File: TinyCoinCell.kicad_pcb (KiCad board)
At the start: 4 copper layers, 23.8 x 24 mm, 51 parts, among them SW1 SW_Push, U1 nRF54L15-QFAA, U2 ADXL367, U8 nPM2100-QEXX, X1 32MHz, X2 32.768kHz

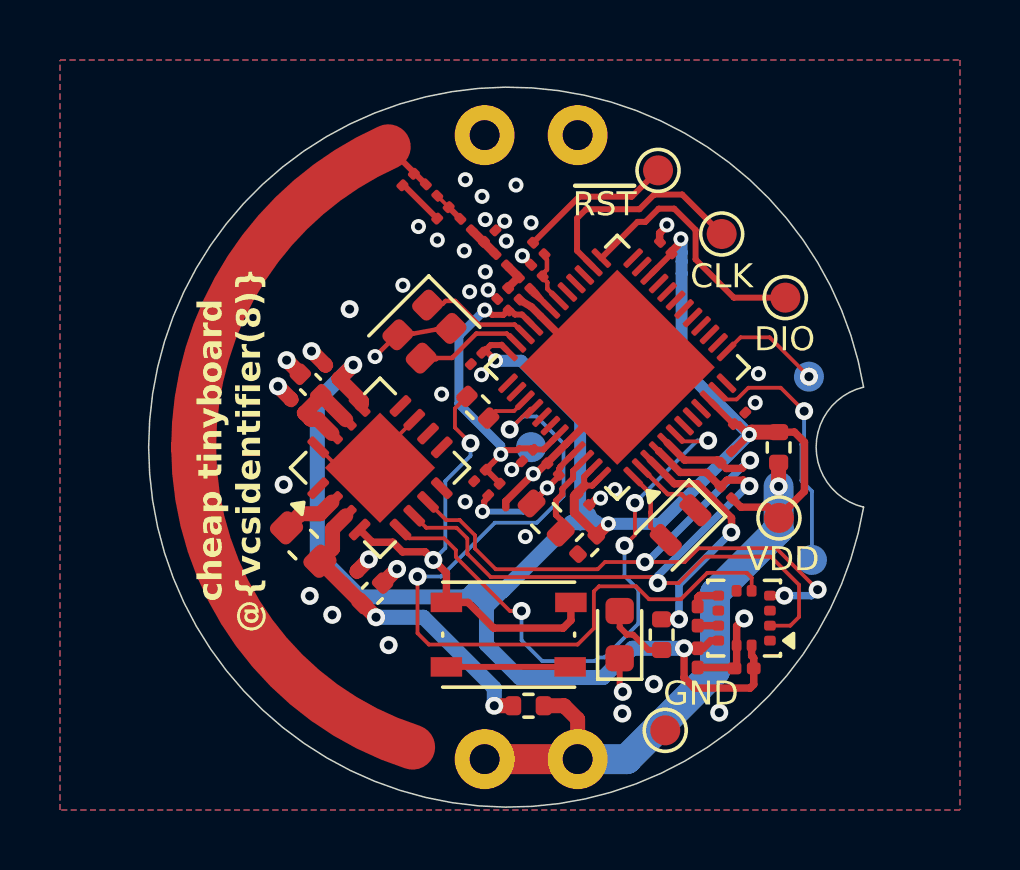
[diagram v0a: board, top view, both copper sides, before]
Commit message: Document TinyCoinCell v2 release
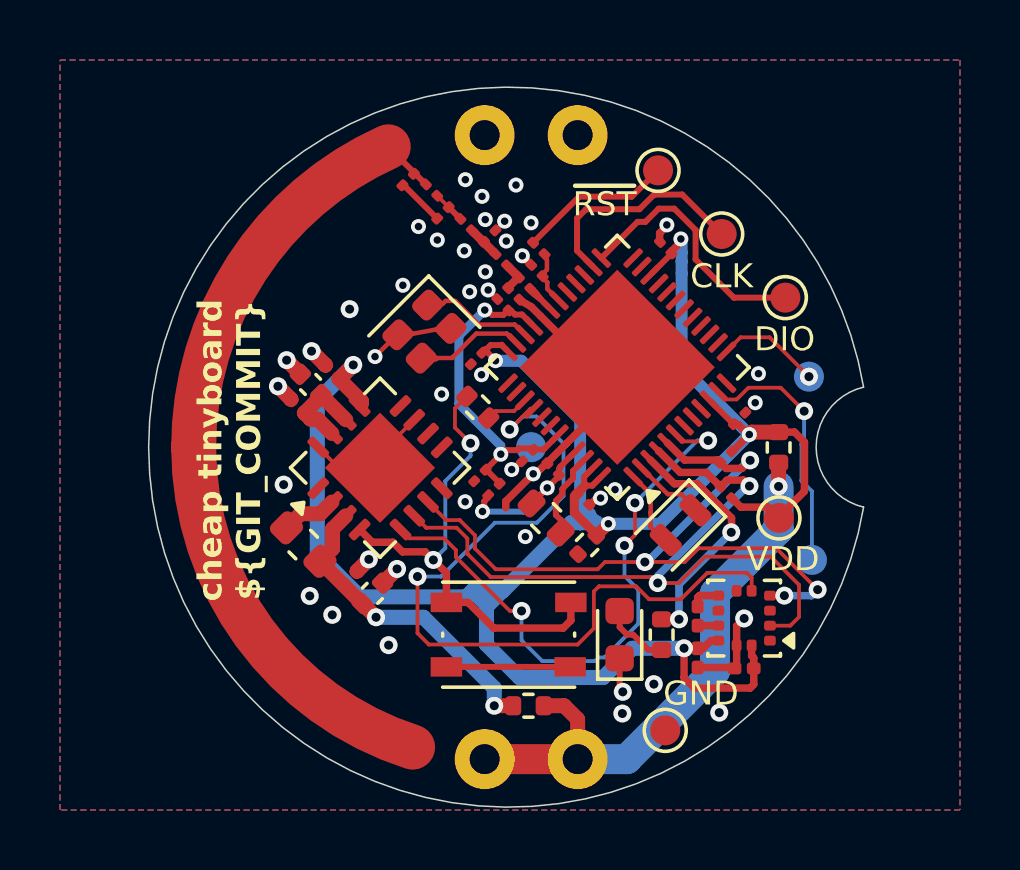
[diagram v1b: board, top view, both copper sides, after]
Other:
- board text added: "cheap tinyboard ${GIT_COMMIT}"
- board text removed: "cheap tinyboard @{vcsidentifier(8)}"
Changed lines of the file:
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@@
 		)
 	)
-	(gr_text "cheap tinyboard \n@{vcsidentifier(8)}\n"
+	(gr_text "cheap tinyboard \n${GIT_COMMIT}\n"
 		(at 134.49516 112.19522 90)
 		(layer "F.SilkS")

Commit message: Updated PCB
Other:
- board text added: "cheap tinyboard @{vcsidentifier(8)}"
- board text removed: "cheap tinyboard ${GIT_COMMIT}"
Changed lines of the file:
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@@
 		)
 	)
-	(gr_text "cheap tinyboard \n${GIT_COMMIT}\n"
+	(gr_text "cheap tinyboard \n@{vcsidentifier(8)}\n"
 		(at 134.49516 112.19522 90)
 		(layer "F.SilkS")
